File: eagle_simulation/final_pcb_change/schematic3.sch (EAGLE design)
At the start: 11 parts, among them U3 R-78E5.0-1.0

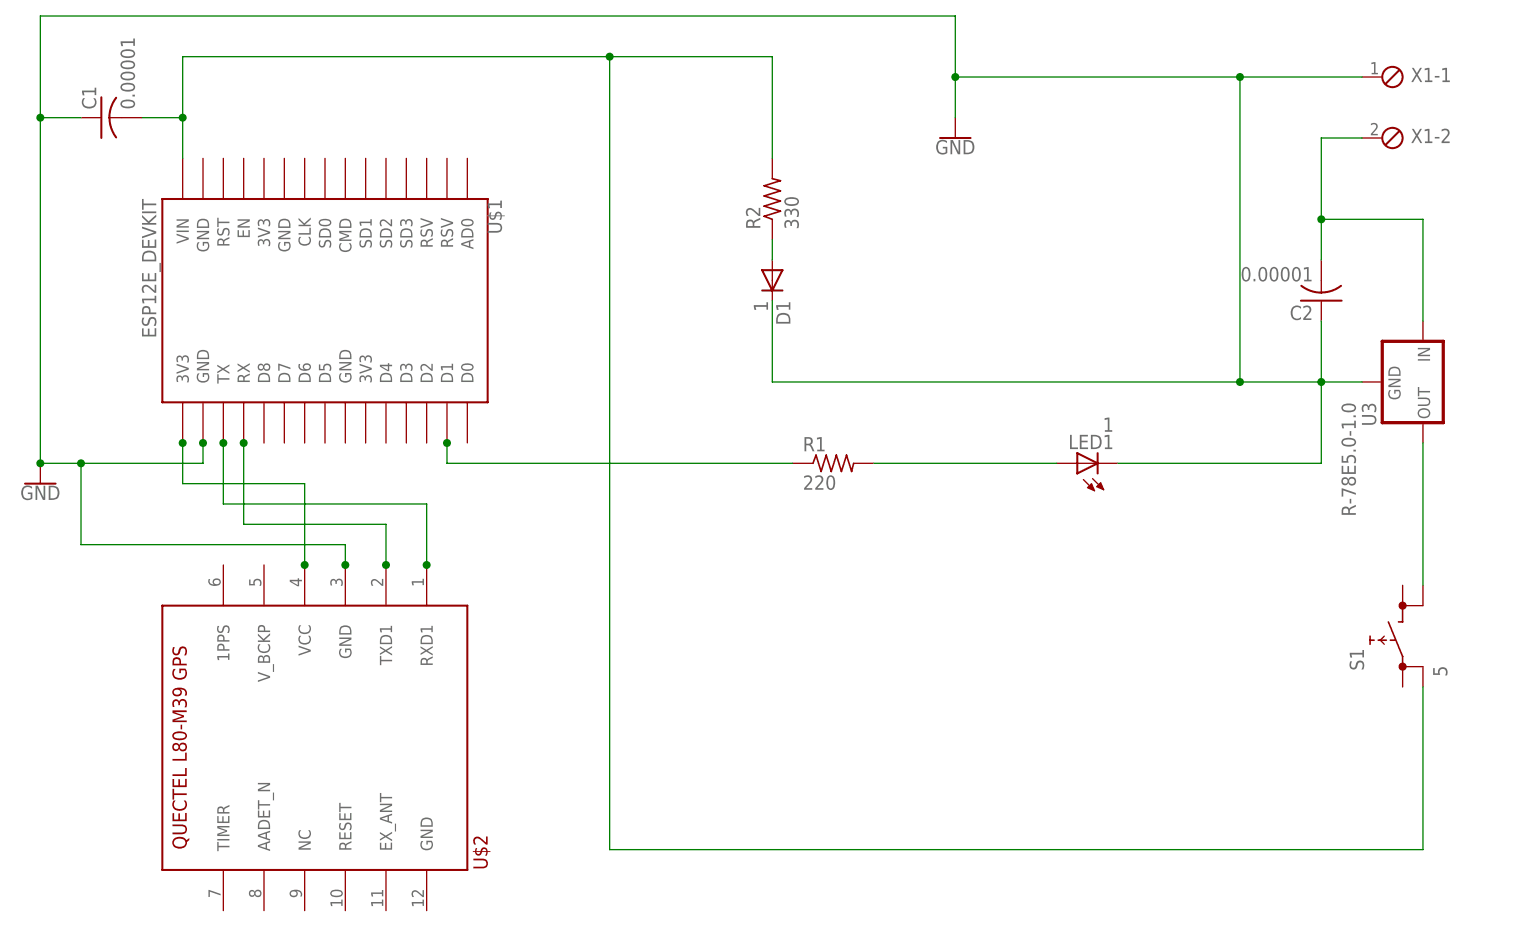
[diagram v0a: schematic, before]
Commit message: edited forgot-password.php and added some files
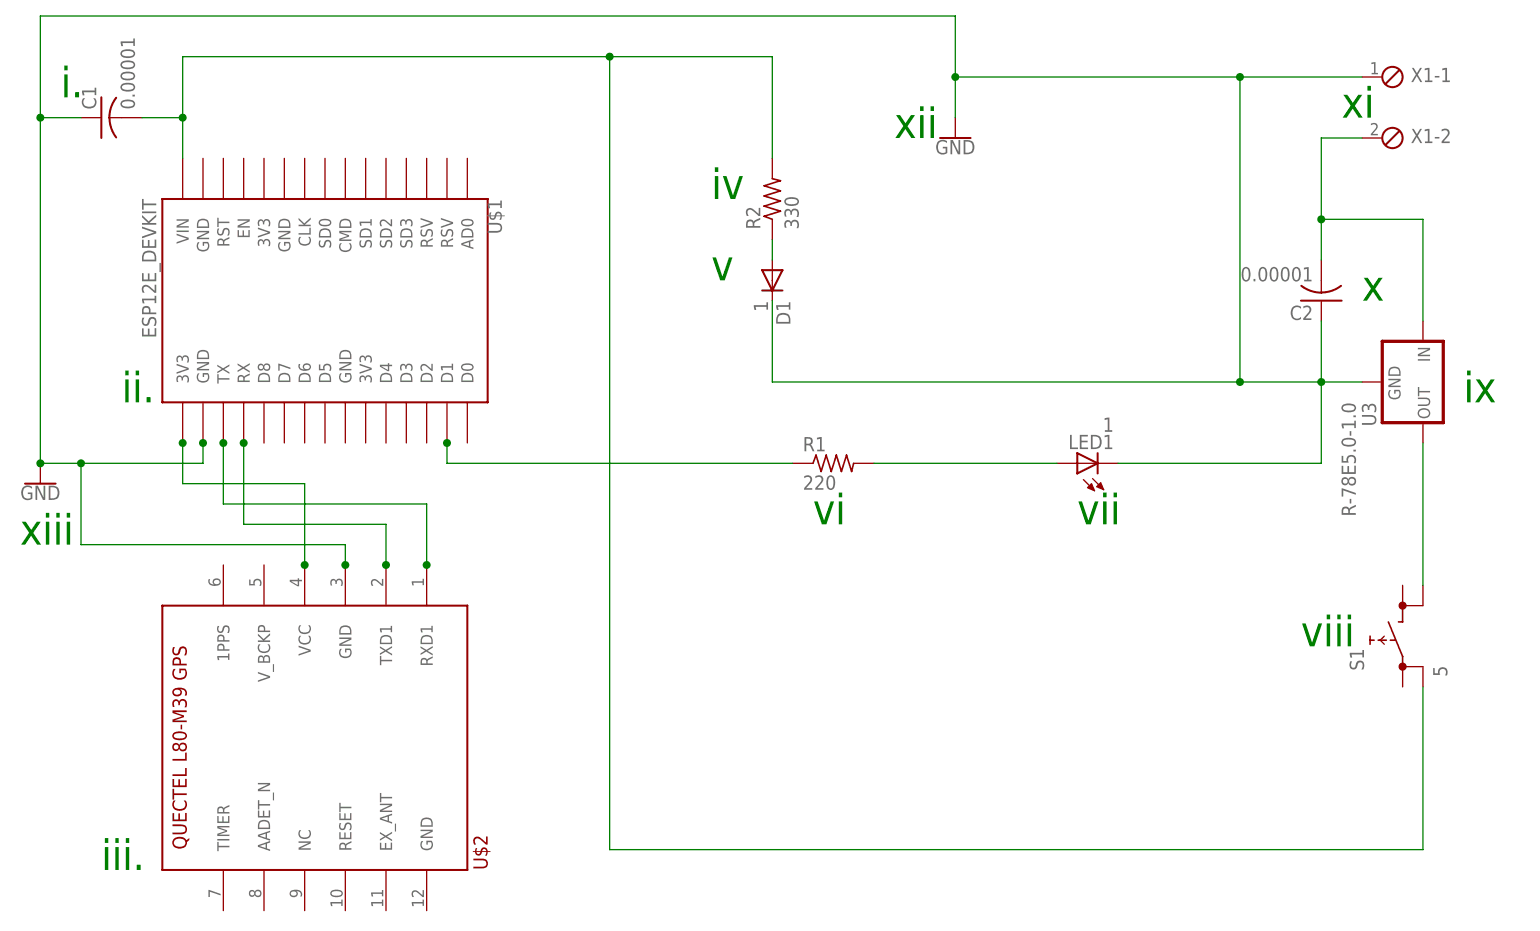
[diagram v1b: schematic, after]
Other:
- note added: "i."
- note added: "ii."
- note added: "iii."
- note added: "iv"
- note added: "ix"
- note added: "v"
- note added: "vi"
- note added: "vii"
- note added: "viii"
- note added: "x"
- note added: "xi"
- note added: "xii"
- note added: "xiii"
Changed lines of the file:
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@@
 <sheet>
 <plain>
+<text x="-12.7" y="91.44" size="3.81" layer="91">i.</text>
+<text x="-5.08" y="53.34" size="3.81" layer="91">ii.</text>
+<text x="-7.62" y="-5.08" size="3.81" layer="91">iii.</text>
+<text x="68.58" y="78.74" size="3.81" layer="91">iv</text>
+<text x="68.58" y="68.58" size="3.81" layer="91">v</text>
+<text x="81.28" y="38.1" size="3.81" layer="91">vi</text>
+<text x="114.3" y="38.1" size="3.81" layer="91">vii</text>
+<text x="142.24" y="22.86" size="3.81" layer="91">viii</text>
+<text x="162.56" y="53.34" size="3.81" layer="91">ix</text>
+<text x="149.86" y="66.04" size="3.81" layer="91">x</text>
+<text x="147.32" y="88.9" size="3.81" layer="91">xi</text>
+<text x="91.44" y="86.36" size="3.81" layer="91">xii</text>
+<text x="-17.78" y="35.56" size="3.81" layer="91">xiii</text>
 </plain>
 <instances>
